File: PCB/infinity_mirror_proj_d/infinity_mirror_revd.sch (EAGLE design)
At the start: 17 parts, among them J1 5.5x2.1mm Barrel, Q1 800mA/40V, Q2 800mA/40V, U1 3.3LDO

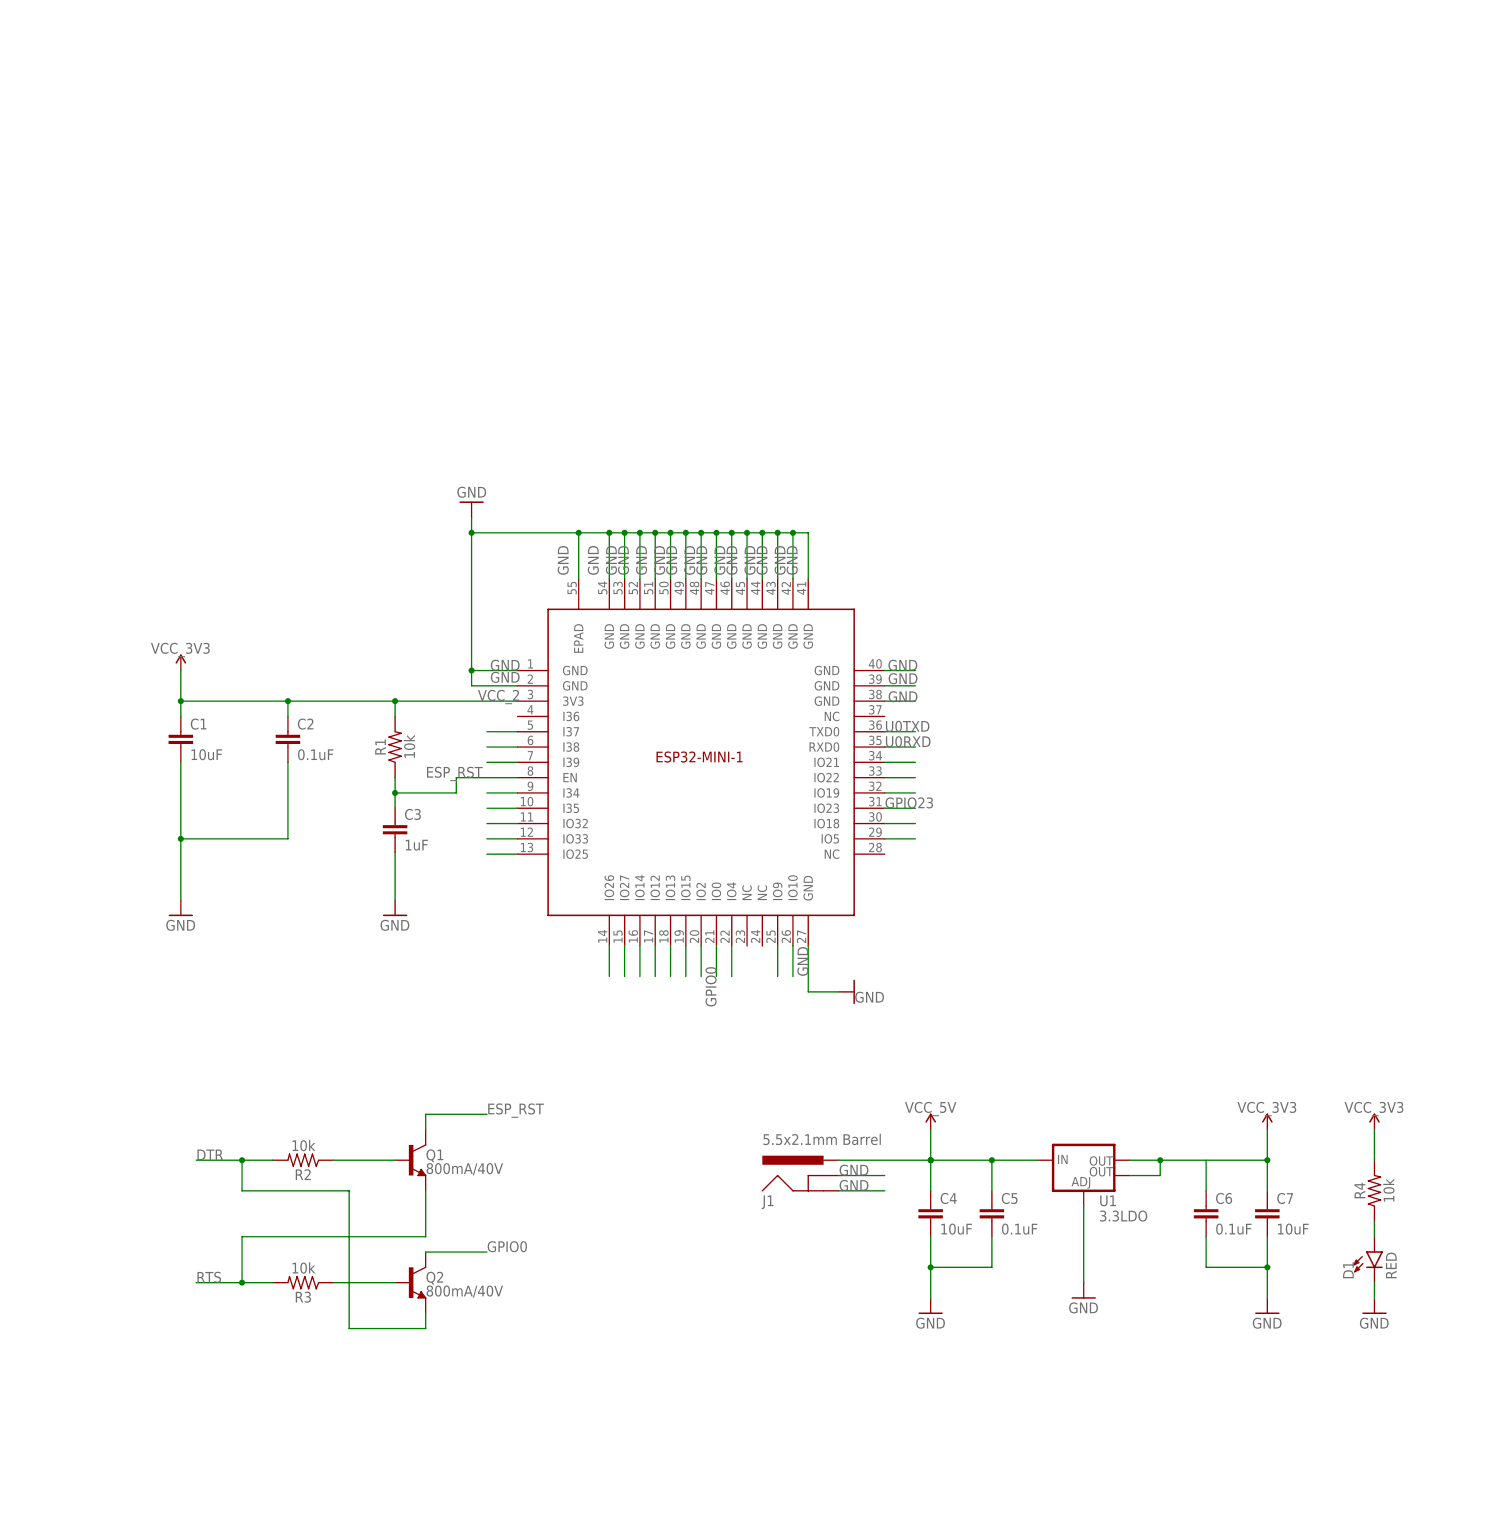
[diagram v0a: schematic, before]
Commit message: 1st draft schematic and board complete, needs review
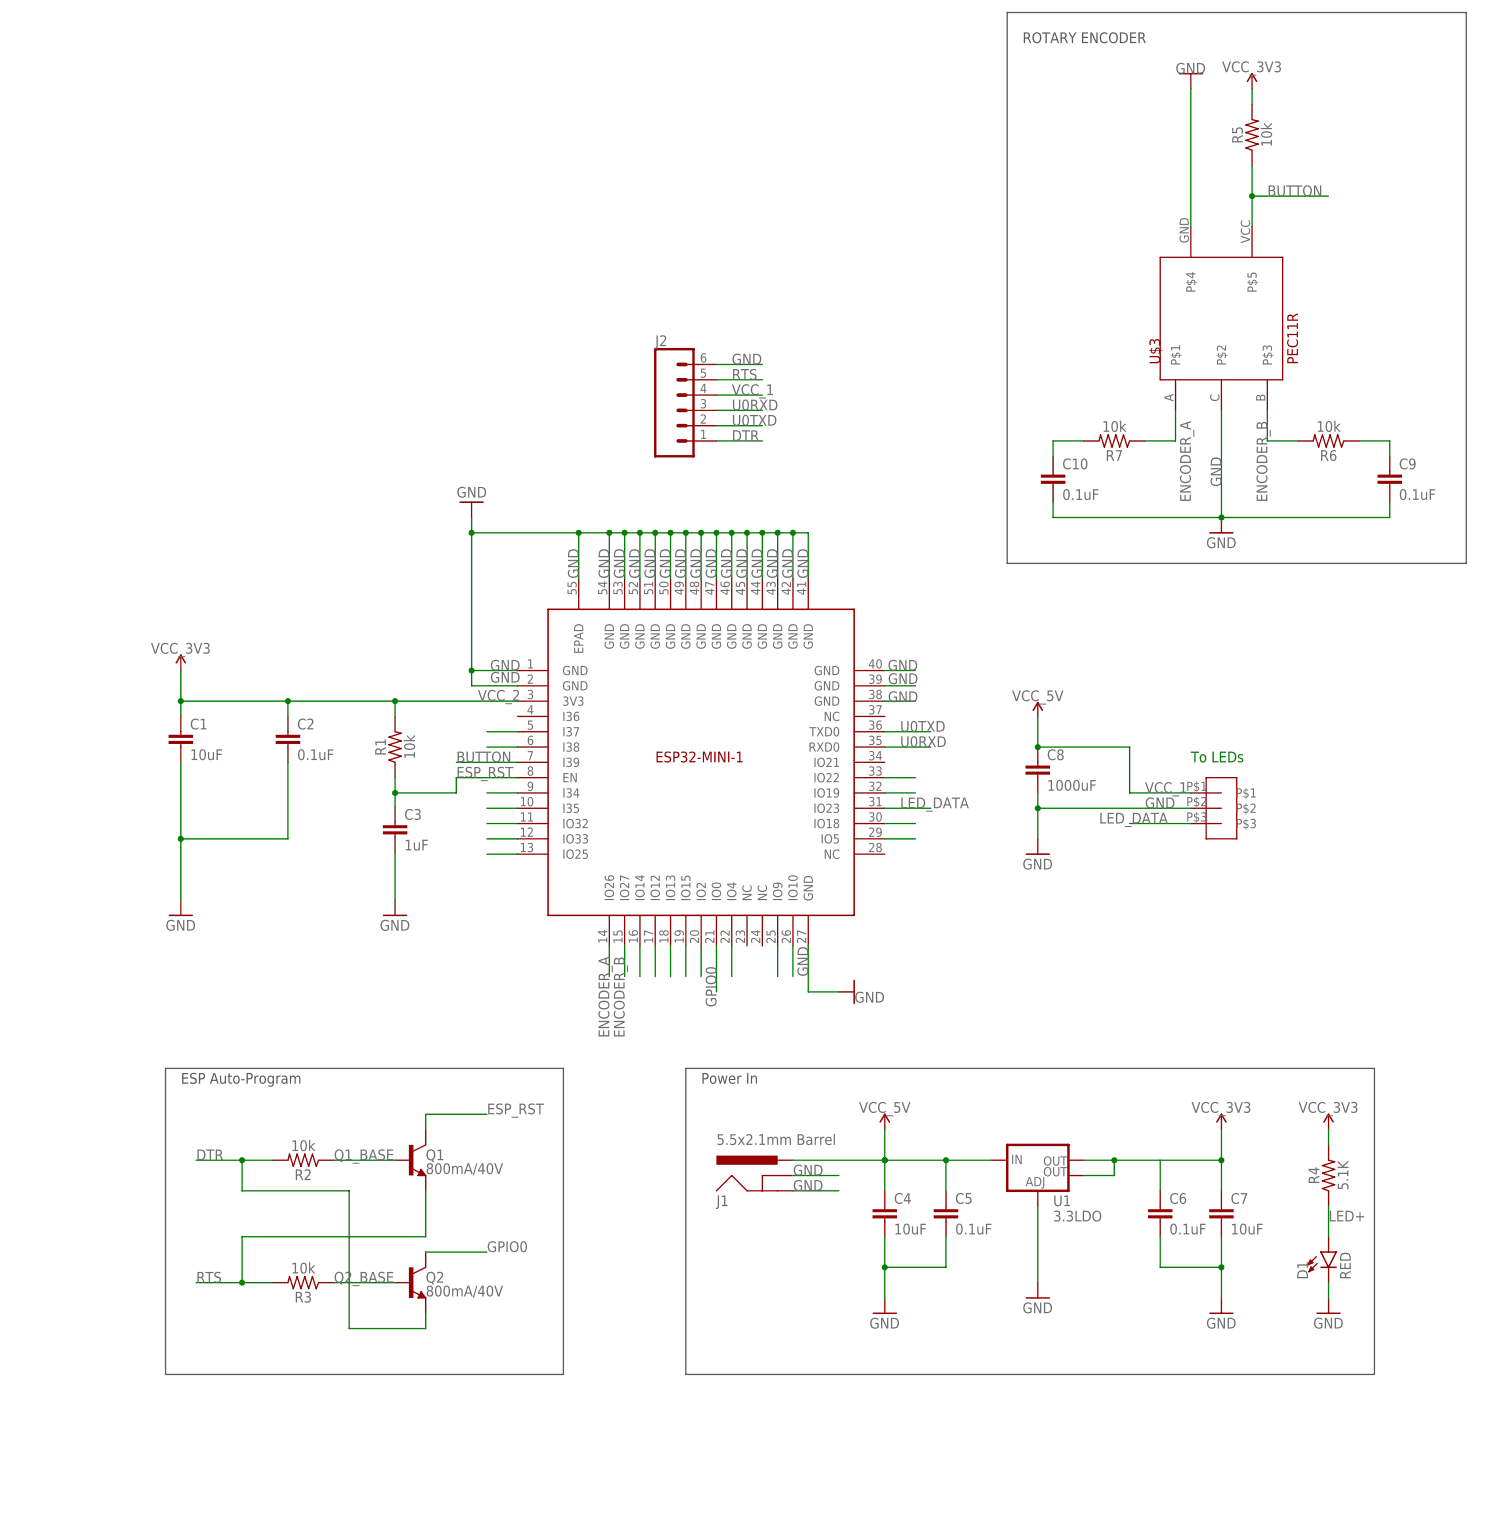
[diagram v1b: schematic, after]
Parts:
- added C10, C9: 0.1uF, _111_IH:CAPACITOR
- added C8: 1000uF, _111_IH:CAPACITOR
- added J2: (no value), SparkFun-Connectors:CONN_06SILK_FEMALE_PTH
- added R5, R6, R7: 10k, _111_IH:RESISTOR
- added U$2: 3-PIN-JST, infinity_mirror_revd:3-PIN-JST
- added U$3: PEC11R, infinity_mirror_revd:PEC11R_ROTARY_ENCODER
- R4: value 10k -> 5.1K
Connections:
- net N$1 renamed Q1_BASE
- net N$2 renamed LED+
- net N$3 renamed Q2_BASE
- removed net GPIO23: U$1.IO23
- removed net N$22: U$1.IO21
- removed net N$35: U$1.IO27
- removed net N$36: U$1.IO26
- removed net N$7: U$1.I39
- new net BUTTON: R5.1, U$1.I39, U$3.P$5
- new net ENCODER_A: R7.1, U$1.IO26, U$3.P$1
- new net ENCODER_B: R6.2, U$1.IO27, U$3.P$3
- new net LED_DATA: U$1.IO23, U$2.P$3
- new net N$15: C10.1, R7.2
- new net N$19: C9.1, R6.1
- net DTR: now also J2.1
- net GND: now also C10.2, C8.2, C9.2, J2.6, U$2.P$2, U$3.P$2, U$3.P$4
- net RTS: now also J2.5
- net U0RXD: now also J2.3
- net U0TXD: now also J2.2
- net VCC_1: now also C8.1, J2.4, U$2.P$1
- net VCC_2: now also R5.2
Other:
- note added: "ESP Auto-Program"
- note added: "Power In"
- note added: "ROTARY ENCODER"
- note added: "To LEDs"
- moved on the sheet: C4, C5, C6, C7, D1, J1, R4, U1

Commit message: fixed encoder schematic
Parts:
- added R8, R9: 10k, _111_IH:RESISTOR
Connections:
- removed net ENCODER_A: R7.1, U$1.IO26, U$3.P$1
- removed net ENCODER_B: R6.2, U$1.IO27, U$3.P$3
- removed net N$15: C10.1, R7.2
- removed net N$19: C9.1, R6.1
- new net ENC_A: C10.1, R7.2, U$1.IO26
- new net ENC_B: C9.1, R6.1, U$1.IO27
- new net N$2: R6.2, R8.2, U$3.P$3
- new net N$3: R7.1, R9.2, U$3.P$1
- net VCC_2: now also R8.1, R9.1
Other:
- moved on the sheet: J2
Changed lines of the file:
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@@
 <part name="C10" library="_111_IH" deviceset="CAPACITOR" device="" value="0.1uF"/>
 <part name="J2" library="SparkFun-Connectors" deviceset="CONN_06" device="SILK_FEMALE_PTH"/>
+<part name="R8" library="_111_IH" deviceset="RESISTOR" device="" value="10k"/>
+<part name="R9" library="_111_IH" deviceset="RESISTOR" device="" value="10k"/>
+<part name="SUPPLY7" library="SparkFun-PowerSymbols" deviceset="VCC_2" device="" value="VCC_3V3"/>
+<part name="SUPPLY8" library="SparkFun-PowerSymbols" deviceset="VCC_2" device="" value="VCC_3V3"/>
 </parts>
 <sheets>
@@
 <wire x1="-2.54" y1="-50.8" x2="111.76" y2="-50.8" width="0.1524" layer="97"/>
 <text x="-86.36" y="-53.34" size="1.778" layer="97">ESP Auto-Program</text>
-<wire x1="-22.86" y1="-50.8" x2="-88.9" y2="-50.8" width="0.1524" layer="97"/>
-<wire x1="-88.9" y1="-50.8" x2="-88.9" y2="-101.6" width="0.1524" layer="97"/>
-<wire x1="-88.9" y1="-101.6" x2="-22.86" y2="-101.6" width="0.1524" layer="97"/>
+<wire x1="-22.86" y1="-50.8" x2="-114.3" y2="-50.8" width="0.1524" layer="97"/>
+<wire x1="-114.3" y1="-50.8" x2="-114.3" y2="-101.6" width="0.1524" layer="97"/>
+<wire x1="-114.3" y1="-101.6" x2="-22.86" y2="-101.6" width="0.1524" layer="97"/>
 <wire x1="-22.86" y1="-101.6" x2="-22.86" y2="-50.8" width="0.1524" layer="97"/>
-<text x="53.34" y="119.38" size="1.778" layer="97">ROTARY ENCODER</text>
-<wire x1="50.8" y1="33.02" x2="50.8" y2="124.46" width="0.1524" layer="97"/>
-<wire x1="50.8" y1="124.46" x2="127" y2="124.46" width="0.1524" layer="97"/>
-<wire x1="127" y1="124.46" x2="127" y2="33.02" width="0.1524" layer="97"/>
-<wire x1="127" y1="33.02" x2="50.8" y2="33.02" width="0.1524" layer="97"/>
+<text x="48.26" y="119.38" size="1.778" layer="97">ROTARY ENCODER</text>
+<wire x1="43.18" y1="33.02" x2="43.18" y2="124.46" width="0.1524" layer="97"/>
+<wire x1="43.18" y1="124.46" x2="129.54" y2="124.46" width="0.1524" layer="97"/>
+<wire x1="129.54" y1="124.46" x2="129.54" y2="33.02" width="0.1524" layer="97"/>
+<wire x1="129.54" y1="33.02" x2="43.18" y2="33.02" width="0.1524" layer="97"/>
 </plain>
 <instances>
@@
 <attribute name="VALUE" x="59.944" y="43.561" size="1.778" layer="96" font="vector"/>
 </instance>
-<instance part="J2" gate="G$1" x="-2.54" y="58.42" smashed="yes">
-<attribute name="VALUE" x="-7.62" y="48.514" size="1.778" layer="96" font="vector"/>
-<attribute name="NAME" x="-7.62" y="69.088" size="1.778" layer="95" font="vector"/>
+<instance part="J2" gate="G$1" x="-106.68" y="-76.2" smashed="yes">
+<attribute name="VALUE" x="-111.76" y="-86.106" size="1.778" layer="96" font="vector"/>
+<attribute name="NAME" x="-111.76" y="-65.532" size="1.778" layer="95" font="vector"/>
+</instance>
+<instance part="R8" gate="G$1" x="109.22" y="68.58" smashed="yes" rot="R270">
+<attribute name="NAME" x="110.744" y="68.58" size="1.778" layer="95" font="vector" rot="R270" align="bottom-center"/>
+<attribute name="VALUE" x="107.696" y="68.58" size="1.778" layer="96" font="vector" rot="R270" align="top-center"/>
+</instance>
+<instance part="R9" gate="G$1" x="63.5" y="68.58" smashed="yes" rot="R270">
+<attribute name="NAME" x="65.024" y="68.58" size="1.778" layer="95" font="vector" rot="R270" align="bottom-center"/>
+<attribute name="VALUE" x="61.976" y="68.58" size="1.778" layer="96" font="vector" rot="R270" align="top-center"/>
+</instance>
+<instance part="SUPPLY7" gate="G$1" x="63.5" y="78.74" smashed="yes">
+<attribute name="VALUE" x="63.5" y="81.534" size="1.778" layer="96" align="bottom-center"/>
+</instance>
+<instance part="SUPPLY8" gate="G$1" x="109.22" y="78.74" smashed="yes">
+<attribute name="VALUE" x="109.22" y="81.534" size="1.778" layer="96" align="bottom-center"/>
 </instance>
 </instances>
@@
 <segment>
 <pinref part="J2" gate="G$1" pin="2"/>
-<wire x1="2.54" y1="55.88" x2="10.16" y2="55.88" width="0.1524" layer="91"/>
-<label x="5.08" y="55.88" size="1.778" layer="95"/>
+<wire x1="-101.6" y1="-78.74" x2="-93.98" y2="-78.74" width="0.1524" layer="91"/>
+<label x="-99.06" y="-78.74" size="1.778" layer="95"/>
 </segment>
 </net>
@@
 </segment>
 </net>
-<net name="ENCODER_B" class="0">
-<segment>
-<wire x1="-12.7" y1="-30.48" x2="-12.7" y2="-35.56" width="0.1524" layer="91"/>
-<pinref part="U$1" gate="G$1" pin="IO27"/>
-<label x="-12.7" y="-45.72" size="1.778" layer="95" rot="R90"/>
-</segment>
-<segment>
-<pinref part="U$3" gate="G$1" pin="P$3"/>
-<wire x1="93.98" y1="58.42" x2="93.98" y2="53.34" width="0.1524" layer="91"/>
-<pinref part="R6" gate="G$1" pin="2"/>
-<wire x1="99.06" y1="53.34" x2="93.98" y2="53.34" width="0.1524" layer="91"/>
-<label x="93.98" y="43.18" size="1.778" layer="95" rot="R90"/>
-</segment>
-</net>
-<net name="ENCODER_A" class="0">
-<segment>
-<wire x1="-15.24" y1="-30.48" x2="-15.24" y2="-35.56" width="0.1524" layer="91"/>
-<pinref part="U$1" gate="G$1" pin="IO26"/>
-<label x="-15.24" y="-45.72" size="1.778" layer="95" rot="R90"/>
-</segment>
+<net name="N$3" class="0">
 <segment>
 <pinref part="U$3" gate="G$1" pin="P$1"/>
@@
 <pinref part="R7" gate="G$1" pin="1"/>
 <wire x1="73.66" y1="53.34" x2="78.74" y2="53.34" width="0.1524" layer="91"/>
-<label x="81.28" y="43.18" size="1.778" layer="95" rot="R90"/>
+<pinref part="R9" gate="G$1" pin="2"/>
+<wire x1="63.5" y1="63.5" x2="63.5" y2="58.42" width="0.1524" layer="91"/>
+<wire x1="63.5" y1="58.42" x2="78.74" y2="58.42" width="0.1524" layer="91"/>
+<junction x="78.74" y="58.42"/>
 </segment>
 </net>
@@
 <segment>
 <pinref part="J2" gate="G$1" pin="6"/>
-<wire x1="2.54" y1="66.04" x2="10.16" y2="66.04" width="0.1524" layer="91"/>
-<label x="5.08" y="66.04" size="1.778" layer="95"/>
+<wire x1="-101.6" y1="-68.58" x2="-93.98" y2="-68.58" width="0.1524" layer="91"/>
+<label x="-99.06" y="-68.58" size="1.778" layer="95"/>
 </segment>
 </net>
@@
 <segment>
 <pinref part="J2" gate="G$1" pin="3"/>
-<wire x1="2.54" y1="58.42" x2="10.16" y2="58.42" width="0.1524" layer="91"/>
-<label x="5.08" y="58.42" size="1.778" layer="95"/>
+<wire x1="-101.6" y1="-76.2" x2="-93.98" y2="-76.2" width="0.1524" layer="91"/>
+<label x="-99.06" y="-76.2" size="1.778" layer="95"/>
 </segment>
 </net>
@@
 <segment>
 <pinref part="J2" gate="G$1" pin="1"/>
-<wire x1="2.54" y1="53.34" x2="10.16" y2="53.34" width="0.1524" layer="91"/>
-<label x="5.08" y="53.34" size="1.778" layer="95"/>
+<wire x1="-101.6" y1="-81.28" x2="-93.98" y2="-81.28" width="0.1524" layer="91"/>
+<label x="-99.06" y="-81.28" size="1.778" layer="95"/>
 </segment>
 </net>
@@
 <segment>
 <pinref part="J2" gate="G$1" pin="5"/>
-<wire x1="2.54" y1="63.5" x2="10.16" y2="63.5" width="0.1524" layer="91"/>
-<label x="5.08" y="63.5" size="1.778" layer="95"/>
+<wire x1="-101.6" y1="-71.12" x2="-93.98" y2="-71.12" width="0.1524" layer="91"/>
+<label x="-99.06" y="-71.12" size="1.778" layer="95"/>
 </segment>
 </net>
@@
 <wire x1="91.44" y1="111.76" x2="91.44" y2="109.22" width="0.1524" layer="91"/>
 </segment>
+<segment>
+<pinref part="R9" gate="G$1" pin="1"/>
+<pinref part="SUPPLY7" gate="G$1" pin="VCC_2"/>
+<wire x1="63.5" y1="73.66" x2="63.5" y2="78.74" width="0.1524" layer="91"/>
+</segment>
+<segment>
+<pinref part="R8" gate="G$1" pin="1"/>
+<pinref part="SUPPLY8" gate="G$1" pin="VCC_2"/>
+<wire x1="109.22" y1="73.66" x2="109.22" y2="78.74" width="0.1524" layer="91"/>
+</segment>
 </net>
 <net name="VCC_1" class="0">
@@
 <segment>
 <pinref part="J2" gate="G$1" pin="4"/>
-<wire x1="2.54" y1="60.96" x2="10.16" y2="60.96" width="0.1524" layer="91"/>
-<label x="5.08" y="60.96" size="1.778" layer="95"/>
+<wire x1="-101.6" y1="-73.66" x2="-93.98" y2="-73.66" width="0.1524" layer="91"/>
+<label x="-99.06" y="-73.66" size="1.778" layer="95"/>
 </segment>
 </net>
@@
 </segment>
 </net>
-<net name="N$15" class="0">
+<net name="ENC_A" class="0">
 <segment>
 <pinref part="C10" gate="G$1" pin="1"/>
@@
 <pinref part="R7" gate="G$1" pin="2"/>
 <wire x1="58.42" y1="53.34" x2="63.5" y2="53.34" width="0.1524" layer="91"/>
-</segment>
-</net>
-<net name="N$19" class="0">
+<wire x1="58.42" y1="53.34" x2="48.26" y2="53.34" width="0.1524" layer="91"/>
+<junction x="58.42" y="53.34"/>
+<label x="48.26" y="53.34" size="1.778" layer="95"/>
+</segment>
+<segment>
+<wire x1="-15.24" y1="-30.48" x2="-15.24" y2="-35.56" width="0.1524" layer="91"/>
+<pinref part="U$1" gate="G$1" pin="IO26"/>
+<label x="-15.24" y="-40.64" size="1.778" layer="95" rot="R90"/>
+</segment>
+</net>
+<net name="ENC_B" class="0">
 <segment>
 <pinref part="R6" gate="G$1" pin="1"/>
@@
 <pinref part="C9" gate="G$1" pin="1"/>
 <wire x1="114.3" y1="53.34" x2="114.3" y2="50.8" width="0.1524" layer="91"/>
+<wire x1="114.3" y1="53.34" x2="124.46" y2="53.34" width="0.1524" layer="91"/>
+<junction x="114.3" y="53.34"/>
+<label x="116.84" y="53.34" size="1.778" layer="95"/>
+</segment>
+<segment>
+<wire x1="-12.7" y1="-30.48" x2="-12.7" y2="-35.56" width="0.1524" layer="91"/>
+<pinref part="U$1" gate="G$1" pin="IO27"/>
+<label x="-12.7" y="-40.64" size="1.778" layer="95" rot="R90"/>
 </segment>
 </net>
@@
 </segment>
 </net>
+<net name="N$2" class="0">
+<segment>
+<pinref part="U$3" gate="G$1" pin="P$3"/>
+<wire x1="93.98" y1="58.42" x2="93.98" y2="53.34" width="0.1524" layer="91"/>
+<pinref part="R6" gate="G$1" pin="2"/>
+<wire x1="99.06" y1="53.34" x2="93.98" y2="53.34" width="0.1524" layer="91"/>
+<wire x1="93.98" y1="58.42" x2="109.22" y2="58.42" width="0.1524" layer="91"/>
+<junction x="93.98" y="58.42"/>
+<pinref part="R8" gate="G$1" pin="2"/>
+<wire x1="109.22" y1="58.42" x2="109.22" y2="63.5" width="0.1524" layer="91"/>
+</segment>
+</net>
